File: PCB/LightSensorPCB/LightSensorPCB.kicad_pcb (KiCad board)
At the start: 2 copper layers, 1 part, among them J1 POWER/I2C

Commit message: Light detection PCB
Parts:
- added C1: 1 uF 6.3V X7R 0402, Capacitor_SMD:C_0402_1005Metric, F.Cu at (159.5, 82.5)
- added D1: RED 1.8V 2mA, LED_SMD:LED_0603_1608Metric, F.Cu at (158.6, 86.5)
- added R1: 10kOhm 1% 0402, Resistor_SMD:R_0402_1005Metric, F.Cu at (165.1, 82.5)
- added R2: 10kOhm 1% 0402, Resistor_SMD:R_0402_1005Metric, F.Cu at (165.1, 84.0)
- added R3: 750Ohm 1% 0402, Resistor_SMD:R_0402_1005Metric, F.Cu at (159.5, 84.4)
- added U1: LTR-329ALS-01, Customs:LTR-329ALS-01, F.Cu at (162.2, 83.3)

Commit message: Light detection PCB finished
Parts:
- added H1: M3, MountingHole:MountingHole_3.2mm_M3_DIN965_Pad, F.Cu at (116.5, 103.5)
- added H2: M3, MountingHole:MountingHole_3.2mm_M3_DIN965_Pad, F.Cu at (103.5, 103.5)
- J1: footprint Connector_Molex:Molex_Micro-Fit_3.0_43045-0412_2x02_P3.00mm_Vertical -> Connector_JST:JST_GH_SM04B-GHS-TB_1x04-1MP_P1.25mm_Horizontal
- moved R3 61.9 mm to (104.0, 111.8), turned to 180 degrees
- moved D1 61.3 mm to (103.5, 113.2), turned to 0 degrees
- moved C1 57.5 mm to (107.5, 107.0)
- moved U1 57.2 mm to (110.0, 106.5)
- moved R1 56.6 mm to (116.5, 111.5)
- moved R2 56.5 mm to (116.5, 112.9)
- moved J1 44.5 mm to (110.0, 111.8)
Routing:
- net +3.3V: track 0.00 -> 24.1 mm, vias 0 -> 2
- net /SCL: track 0.00 -> 11.2 mm
- net /SDA: track 0.00 -> 9.57 mm
- net Net-(D1-Pad2): track 0.00 -> 1.61 mm
- net GND: vias 0 -> 4
- added copper zone on B.Cu, net GND
- added copper zone on F.Cu, net GND
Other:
- board outline added: 20 x 15 mm

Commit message: Significant PCB progress
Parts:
- removed R1, R2: 10kOhm 1% 0402, Resistor_SMD:R_0402_1005Metric
- added C2: 0.1 uF 50V X7R 0603, Capacitor_SMD:C_0603_1608Metric, F.Cu at (118.0, 120.2)
- added C3: 0.1 uF 50V X7R 0603, Capacitor_SMD:C_0603_1608Metric, F.Cu at (118.0, 118.5)
- added C4: 4.7 uF 6.3V X5R 0603, Capacitor_SMD:C_0603_1608Metric, B.Cu at (118.0, 120.2)
- added C5: 0.1 uF 50V X7R 0603, Capacitor_SMD:C_0603_1608Metric, B.Cu at (118.0, 118.5)
- added R4: 10kOhm 1% 0603, Resistor_SMD:R_0603_1608Metric, B.Cu at (118.8, 110.0)
- added TP1: TestPoint_2Pole, Connector_PinHeader_2.54mm:PinHeader_1x02_P2.54mm_Vertical, B.Cu at (110.0, 105.5)
- added U2: LSM6DSMTR, Customs:PQFN50P300X250X86-14N, F.Cu at (113.4, 119.2)
- added U3: VL53L3CXV0DH/1, Customs:XDCR_VL53L3CXV0DH_1, B.Cu at (118.0, 114.5)
- C1: value 1 uF 6.3V X7R 0402 -> 1 uF 25V X5R 0603; footprint Capacitor_SMD:C_0402_1005Metric -> Capacitor_SMD:C_0603_1608Metric
- D1: value RED 1.8V 2mA -> RED 1.8V 2mA 0603; moved to B.Cu
- J1: footprint Connector_JST:JST_GH_SM04B-GHS-TB_1x04-1MP_P1.25mm_Horizontal -> Connector_Molex:Molex_Micro-Fit_3.0_43045-0400_2x02_P3.00mm_Horizontal; moved to B.Cu
- R3: value 750Ohm 1% 0402 -> 750Ohm 1% 0603; footprint Resistor_SMD:R_0402_1005Metric -> Resistor_SMD:R_0603_1608Metric; moved to B.Cu
- moved H1 13.0 mm to (103.5, 103.5)
- moved H2 13.0 mm to (116.5, 103.5)
- moved R3 10.5 mm to (108.9, 121.0), turned to 0 degrees
- moved D1 7.90 mm to (105.0, 121.0)
- moved C1 7.61 mm to (115.0, 108.3), turned to 90 degrees
- moved U1 3.89 mm to (112.8, 109.2), turned to -90 degrees
- moved J1 1.27 mm to (109.6, 113.0), turned to -90 degrees
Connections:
- J1 pad 1: +3.3V -> /SDA
- J1 pad 3: /SDA -> /SCL
- J1 pad 4: /SCL -> +3.3V
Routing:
- net /GPIO_LSM: track 0.00 -> 19.0 mm
- net +3.3V: track 24.1 -> 42.1 mm, vias 2 -> 1
- net GND: track 0.00 -> 14.9 mm, vias 4 -> 12
- net /GPIO_VL5: track 0.00 -> 14.9 mm
- net /SDA: track 9.57 -> 19.9 mm, vias 0 -> 1
- net /SCL: track 11.2 -> 13.4 mm, vias 0 -> 1
- net Net-(D1-Pad2): track 1.61 -> 2.33 mm
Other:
- board size 20 x 15 mm -> 20 x 23 mm
- board text added: "+3.3V"
- board text added: "23 x 20 mm M3 x 13 mm"
- board text added: "Hopper PCB REV A May 2023"
- board text added: "INT1"
- board text added: "VL51"

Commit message: Main pcb reviewed
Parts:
- moved U2 0.41 mm to (113.0, 119.2)
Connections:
- R4 pad 2: Net-(R4-Pad2) -> Net-(U3-Pad5)
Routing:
- net /SCL: track 13.4 -> 24.2 mm, vias 1 -> 4
- net +3.3V: track 42.1 -> 51.5 mm, vias 1 -> 0
- net /SDA: track 19.9 -> 24.2 mm, vias 1 -> 4
- net Net-(U3-Pad5): track 0.00 -> 2.10 mm
- net GND: track 14.9 -> 13.0 mm, vias 12 -> 20
- net (no net): vias 0 -> 1
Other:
- board text added: "23 x 20 mm H M3x13 mm"
- board text removed: "23 x 20 mm M3 x 13 mm"

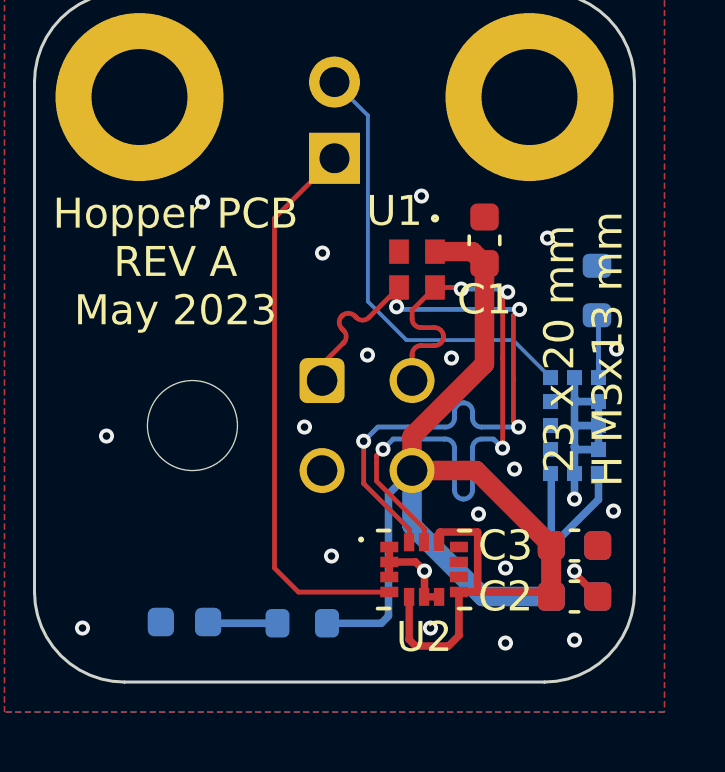
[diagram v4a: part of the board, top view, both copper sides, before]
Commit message: 3x PCB ready for gerberization
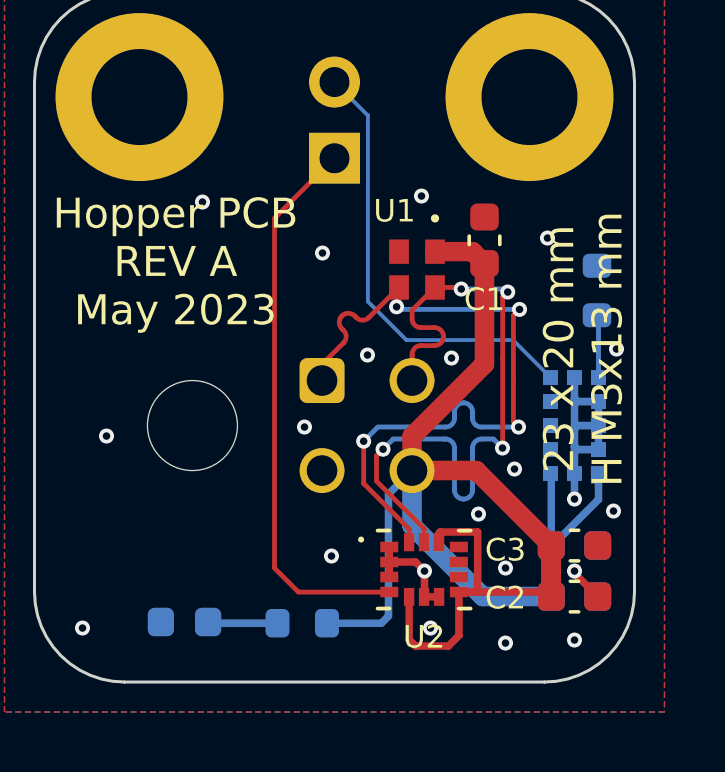
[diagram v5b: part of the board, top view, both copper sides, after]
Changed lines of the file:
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@@
     (attr smd)
     (fp_text reference "U2" (at 0 2.25) (layer "F.SilkS")
-      (effects (font (size 1 1) (thickness 0.16)))
+      (effects (font (size 0.75 0.75) (thickness 0.15)))
     )
     (fp_text value "LSM6DSMTR" (at 4.9008 1.9952) (layer "F.Fab")
@@
     (attr through_hole)
     (fp_text reference "U1" (at -1.95 0.75 180) (layer "F.SilkS")
-      (effects (font (size 1 1) (thickness 0.16)))
+      (effects (font (size 0.75 0.75) (thickness 0.15)))
     )
     (fp_text value "LTR-329ALS-01" (at 0 -2.54 90) (layer "F.SilkS") hide
@@
     (attr exclude_from_pos_files)
     (fp_text reference "H1" (at 0 -3.8) (layer "F.SilkS") hide
-      (effects (font (size 1 1) (thickness 0.16)))
+      (effects (font (size 0.75 0.75) (thickness 0.15)))
     )
     (fp_text value "M3" (at 0 3.8) (layer "F.Fab")
@@
     (attr smd)
     (fp_text reference "C1" (at -1.975 0 180) (layer "F.SilkS")
-      (effects (font (size 1 1) (thickness 0.16)))
+      (effects (font (size 0.75 0.75) (thickness 0.15)))
     )
     (fp_text value "1 uF 25V X5R 0603" (at 0 1.43 90) (layer "F.Fab")
@@
     (attr exclude_from_pos_files)
     (fp_text reference "H2" (at 0 -3.8) (layer "F.SilkS") hide
-      (effects (font (size 1 1) (thickness 0.16)))
+      (effects (font (size 0.75 0.75) (thickness 0.15)))
     )
     (fp_text value "M3" (at 0 3.8) (layer "F.Fab")
@@
     (property "Vendor Part Number" "1276-1935-1-ND")
     (attr smd)
-    (fp_text reference "C2" (at 2.3 0) (layer "F.SilkS")
-      (effects (font (size 1 1) (thickness 0.16)))
+    (fp_text reference "C2" (at 2.3 -0.05) (layer "F.SilkS")
+      (effects (font (size 0.75 0.75) (thickness 0.15)))
     )
     (fp_text value "0.1 uF 50V X7R 0603" (at 0 1.43) (layer "F.Fab")
@@
     (property "Vendor Part Number" "1276-1935-1-ND")
     (attr smd)
-    (fp_text reference "C3" (at 2.3 0) (layer "F.SilkS")
-      (effects (font (size 1 1) (thickness 0.16)))
+    (fp_text reference "C3" (at 2.3 -0.15) (layer "F.SilkS")
+      (effects (font (size 0.75 0.75) (thickness 0.15)))
     )
     (fp_text value "0.1 uF 50V X7R 0603" (at 0 1.43) (layer "F.Fab")
@@
     (property "Vendor Part Number" "1276-1045-1-ND")
     (attr smd)
-    (fp_text reference "C4" (at -2.4 0) (layer "B.SilkS")
-      (effects (font (size 1 1) (thickness 0.16)) (justify mirror))
+    (fp_text reference "C4" (at -2.2 0) (layer "B.SilkS")
+      (effects (font (size 0.75 0.75) (thickness 0.15)) (justify mirror))
     )
     (fp_text value "4.7 uF 6.3V X5R 0603" (at 0 -1.43) (layer "B.Fab")
@@
     (attr through_hole)
     (fp_text reference "J1" (at -2.85 -0.115 180) (layer "B.SilkS")
-      (effects (font (size 1 1) (thickness 0.16)) (justify mirror))
+      (effects (font (size 0.75 0.75) (thickness 0.15)) (justify mirror))
     )
     (fp_text value "POWER/I2C" (at 1.5 -5.7 90) (layer "B.Fab")
@@
     (property "Vendor Part Number" "1276-1935-1-ND")
     (attr smd)
-    (fp_text reference "C5" (at -2.4 0) (layer "B.SilkS")
-      (effects (font (size 1 1) (thickness 0.16)) (justify mirror))
+    (fp_text reference "C5" (at -2.2 0) (layer "B.SilkS")
+      (effects (font (size 0.75 0.75) (thickness 0.15)) (justify mirror))
     )
     (fp_text value "0.1 uF 50V X7R 0603" (at 0 -1.43) (layer "B.Fab")
@@
     (attr through_hole)
     (fp_text reference "TP1" (at 0 2.33) (layer "B.SilkS") hide
-      (effects (font (size 1 1) (thickness 0.16)) (justify mirror))
+      (effects (font (size 0.75 0.75) (thickness 0.15)) (justify mirror))
     )
     (fp_text value "TestPoint_2Pole" (at 0 -4.87) (layer "B.Fab")
@@
     (property "Vendor Part Number" "497-VL53L3CXV0DH/1CT-ND")
     (attr smd)
-    (fp_text reference "U3" (at 1.75 -2.4) (layer "B.SilkS")
-      (effects (font (size 1 1) (thickness 0.16)) (justify mirror))
+    (fp_text reference "U3" (at 1.75 -2.2) (layer "B.SilkS")
+      (effects (font (size 0.75 0.75) (thickness 0.15)) (justify mirror))
     )
     (fp_text value "VL53L3CXV0DH/1" (at 8.925 -2.315 270) (layer "B.Fab")
@@
     (property "Vendor Part Number" "846-CSL1901UW1CT-ND")
     (attr smd)
-    (fp_text reference "D1" (at -2.5 0) (layer "B.SilkS")
-      (effects (font (size 1 1) (thickness 0.16)) (justify mirror))
+    (fp_text reference "D1" (at -2.3 0) (layer "B.SilkS")
+      (effects (font (size 0.75 0.75) (thickness 0.15)) (justify mirror))
     )
     (fp_text value "RED 1.8V 2mA 0603" (at 0 -1.43) (layer "B.Fab")
@@
     (property "Vendor Part Number" "RNCP0603FTD10K0CT-ND")
     (attr smd)
-    (fp_text reference "R4" (at -2.25 -0.05) (layer "B.SilkS")
-      (effects (font (size 1 1) (thickness 0.16)) (justify mirror))
+    (fp_text reference "R4" (at -2.05 -0.05) (layer "B.SilkS")
+      (effects (font (size 0.75 0.75) (thickness 0.15)) (justify mirror))
     )
     (fp_text value "10kOhm 1% 0603" (at 0 -1.43 90) (layer "B.Fab")
@@
     (property "Vendor Part Number" "311-750HRCT-ND")
     (attr smd)
-    (fp_text reference "R3" (at 2.475 0) (layer "B.SilkS")
-      (effects (font (size 1 1) (thickness 0.16)) (justify mirror))
+    (fp_text reference "R3" (at 2.275 0) (layer "B.SilkS")
+      (effects (font (size 0.75 0.75) (thickness 0.15)) (justify mirror))
     )
     (fp_text value "750Ohm 1% 0603" (at 0 -1.43) (layer "B.Fab")
@@
   (gr_arc (start 103 123) (mid 100.87868 122.12132) (end 100 120) (layer "Edge.Cuts") (width 0.1))
   (gr_arc (start 120 120) (mid 119.12132 122.12132) (end 117 123) (layer "Edge.Cuts") (width 0.1))
-  (gr_text "INT1" (at 107.7 105.7) (layer "B.SilkS")
-    (effects (font (size 0.5 0.5) (thickness 0.1)) (justify mirror))
-  )
-  (gr_text "VL51" (at 107.6 102.9) (layer "B.SilkS")
-    (effects (font (size 0.5 0.5) (thickness 0.1)) (justify mirror))
+  (gr_text "INT1" (at 108 105.7 90) (layer "B.SilkS")
+    (effects (font (size 0.75 0.75) (thickness 0.15)) (justify mirror))
+  )
+  (gr_text "VL51" (at 108 103 90) (layer "B.SilkS")
+    (effects (font (size 0.75 0.75) (thickness 0.15)) (justify mirror))
   )
   (gr_text "+3.3V" (at 105.3 122.4) (layer "B.SilkS")
